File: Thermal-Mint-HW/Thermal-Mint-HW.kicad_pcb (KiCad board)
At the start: 4 copper layers, 90 x 54 mm, 106 parts, among them J1 Molex_5031821852, J2 USB4110-GF-A, J3 Conn_01x20_Male, J4 Conn_01x12_Male, J5 Conn_Coaxial, J6 Conn_01x03_Female, SW1 PTS647, SW2 PTS647, U1 ADS1220-VQFN, U2 ADS1220-VQFN, U3 SN74LVC138ARSVR, U4 AT25DL081-SSHN-T, U5 NCP1117-3.3_SOT223, U6 MAX7317ATE+, U7 ESP32-C3, Y1 FL4000157Z, Y2 CM8V-T1A-32.768KHZ-12.5PF-20P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

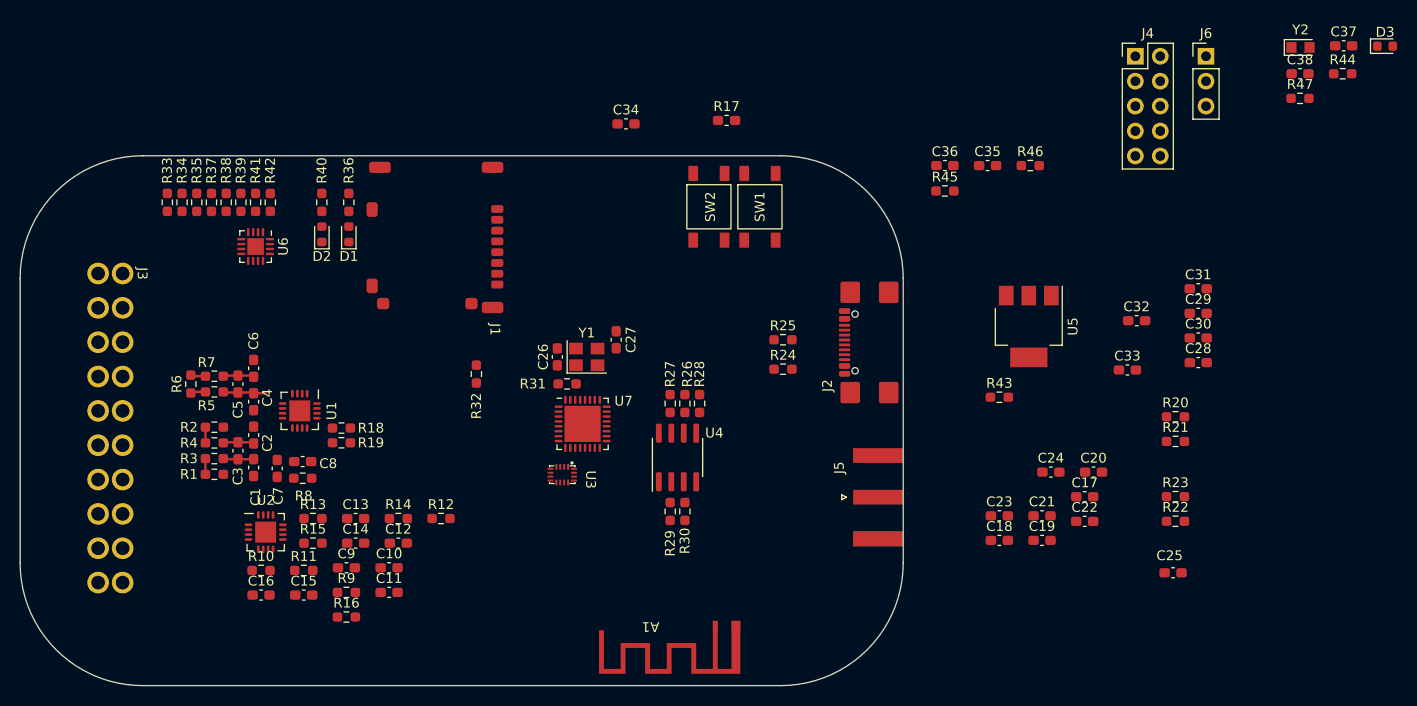
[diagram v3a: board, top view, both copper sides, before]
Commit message: Temporary commit before changing processor from C3 to s2
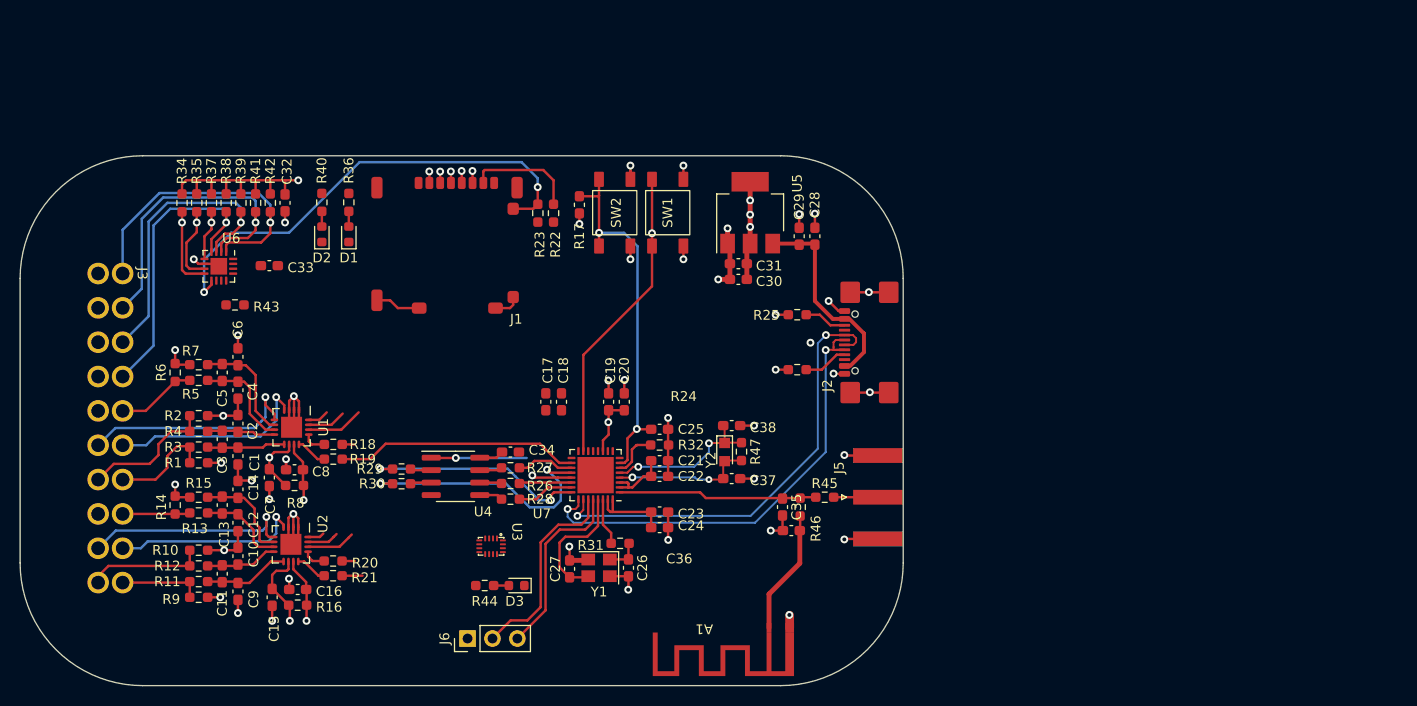
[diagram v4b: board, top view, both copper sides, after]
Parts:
- removed J4: Conn_01x12_Male, Connector_PinHeader_2.54mm:PinHeader_2x05_P2.54mm_Vertical
- removed R33: 1k, Resistor_SMD:R_0603_1608Metric_Pad0.98x0.95mm_HandSolder
- moved D3 104.2 mm to (112.6, 103.8), turned to 180 degrees
- moved R44 101.8 mm to (109.3, 103.8), turned to 180 degrees
- moved J6 95.8 mm to (107.6, 109.2), turned to 90 degrees
- moved C33 88.1 mm to (87.4, 71.2)
- moved C32 87.6 mm to (89.0, 64.8), turned to -90 degrees
- moved R20 87.1 mm to (93.9, 101.3)
- moved R21 86.9 mm to (93.9, 102.8)
- moved R43 78.5 mm to (83.9, 75.2)
- moved C37 76.4 mm to (134.5, 92.9)
- moved Y2 71.7 mm to (133.8, 90.2), turned to -90 degrees
- moved R23 71.1 mm to (114.8, 65.8), turned to 90 degrees
- moved R22 70.7 mm to (116.4, 65.8), turned to -90 degrees
- moved C38 68.1 mm to (134.5, 87.5)
- moved R47 67.3 mm to (135.5, 90.2), turned to -90 degrees
- moved C17 55.8 mm to (115.6, 85.1), turned to 90 degrees
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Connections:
- U2 pad 4: /ADC3AIN3 -> /ADC2AIN3
- U2 pad 5: /ADC2AIN3 -> /ADC2AIN2
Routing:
- net GND: track 1.53 -> 119.4 mm, vias 0 -> 43
- net /GPIO7: track 0.00 -> 48.9 mm, vias 0 -> 2
- net +3V3: track 0.00 -> 48.9 mm, vias 0 -> 8
- net /TM-ESP32/D-: track 0.00 -> 47.4 mm, vias 0 -> 2
- net /TM-ESP32/D+: track 0.00 -> 46.1 mm, vias 0 -> 2
- net +5V: track 0.00 -> 43.7 mm, vias 0 -> 1
- net Net-(U7-CHIP_EN): track 0.00 -> 37.9 mm, vias 0 -> 2
- net /GPIO1: track 0.00 -> 31.5 mm, vias 0 -> 1
- net /GPIO0: track 0.00 -> 31.3 mm, vias 0 -> 1
- net /GPIO2: track 0.00 -> 30.9 mm, vias 0 -> 1
- net /GPIO3: track 0.00 -> 30.7 mm, vias 0 -> 1
- net Net-(U7-GPIO9): track 0.00 -> 30.6 mm, vias 0 -> 1
- net /TM-ESP32/SPIWP: track 0.00 -> 27.5 mm, vias 0 -> 2
- net /nDRDY1: track 0.00 -> 24.8 mm
- net /ADC1AIN2: track 0.00 -> 23.0 mm, vias 0 -> 1
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- added copper zone on In2.Cu, net +3V3
- added copper zone on In1.Cu, net GND
